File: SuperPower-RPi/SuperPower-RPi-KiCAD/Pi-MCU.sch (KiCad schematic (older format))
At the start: 25 parts, among them J5 Conn_01x06, J7 Conn_01x03, J8 Conn_01x10, J9 Conn_01x02, SW1 Tact, U3 STM32F412RETx, U4 ATtiny85-20SU, U5 ME6210A33M3G

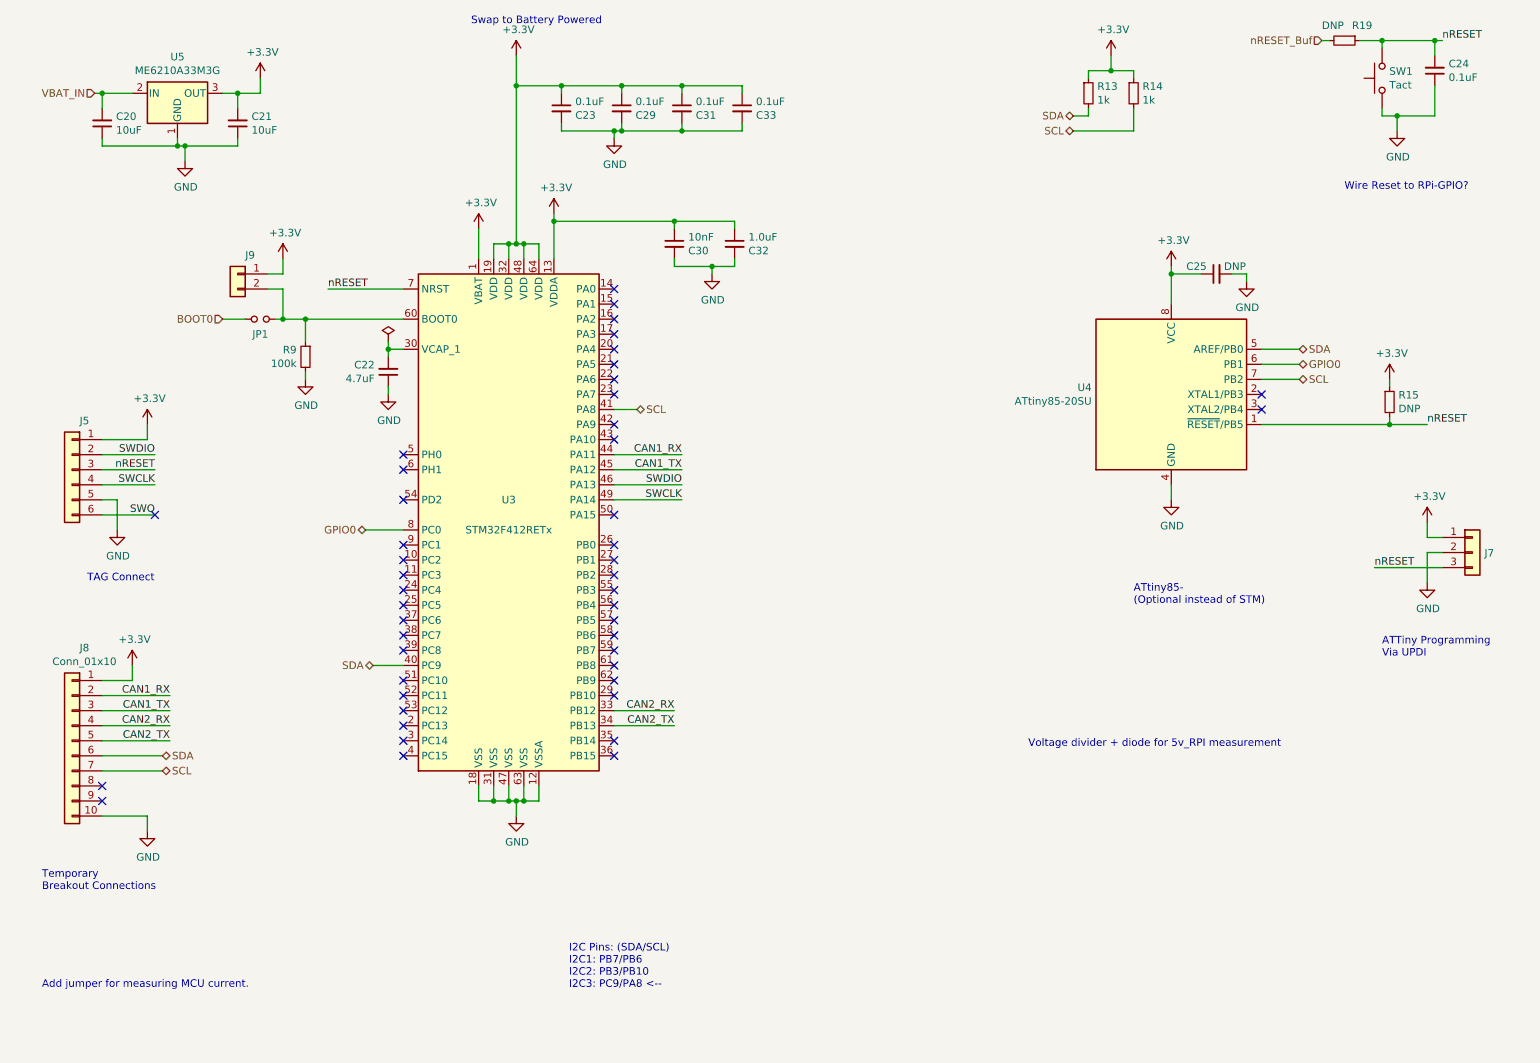
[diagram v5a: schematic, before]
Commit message: Added voltage divider to measure 5V rail.
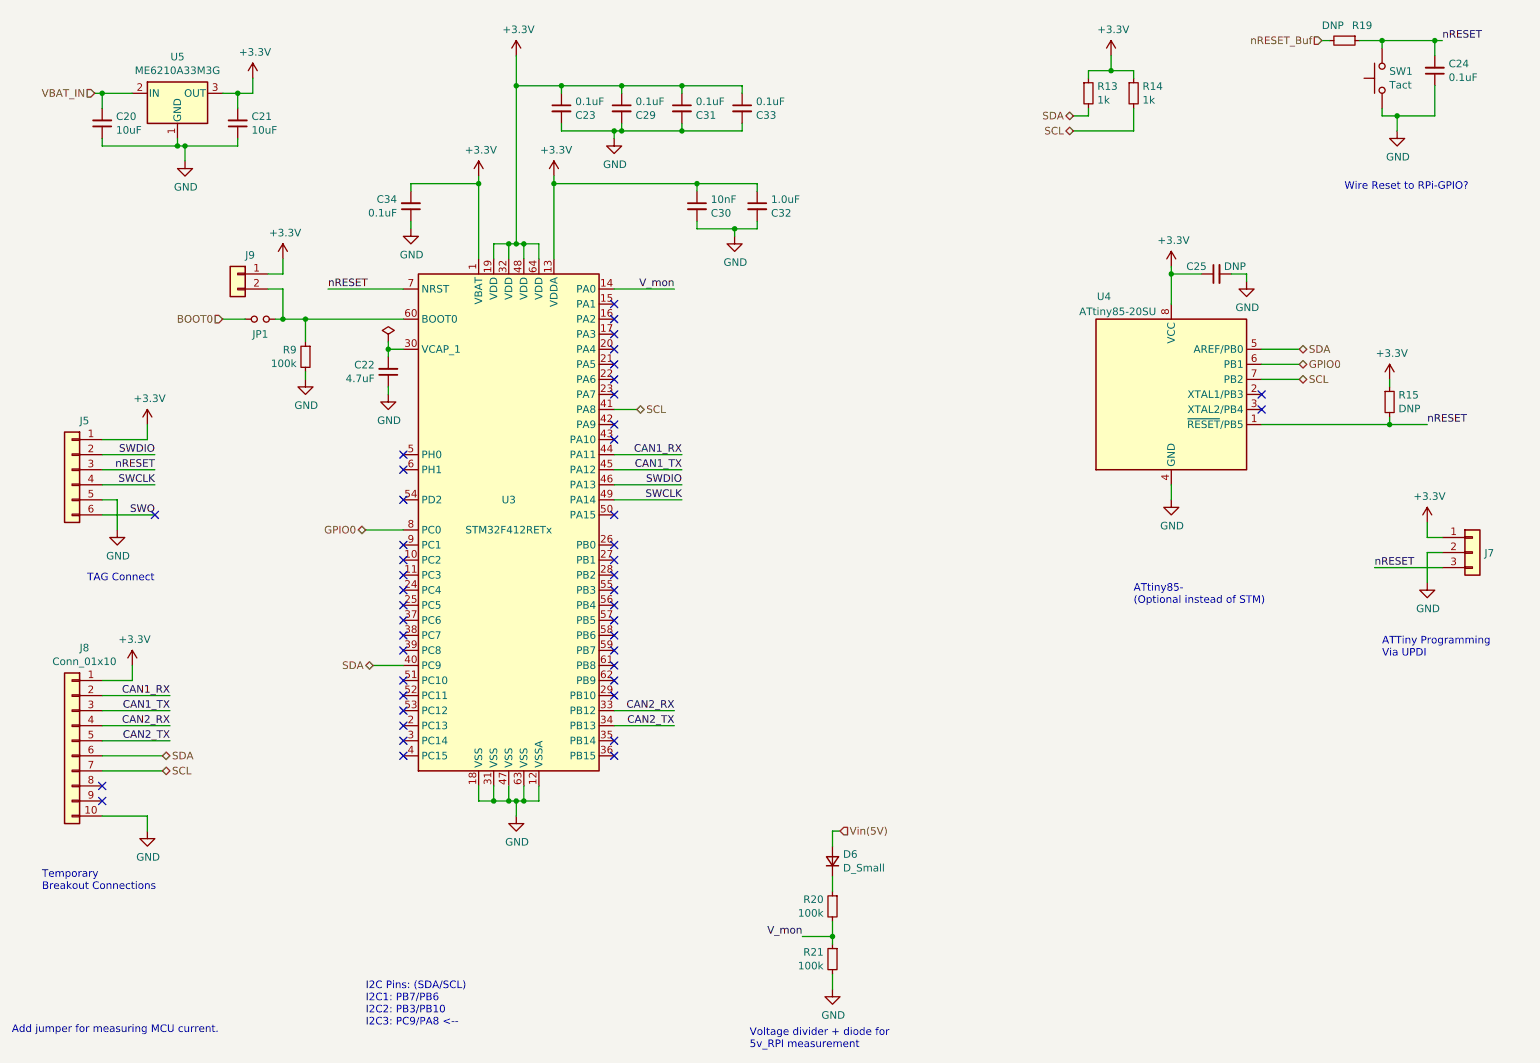
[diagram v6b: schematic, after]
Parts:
- added C34: 0.1uF, Capacitor_SMD:C_0603_1608Metric, symbol Device:C_Small
- added D6: D_Small, Diode_SMD:D_SOD-523, symbol Device:D_Small
- added R20, R21: 100k, Resistor_SMD:R_0603_1608Metric, symbol Device:R_Small
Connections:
- net +3V3: now also C34.2
- net GND: now also C34.1, R21.2
- net V_mon: now reaches U3.14 (PA0)
- net V_mon: now also R20.2, R21.1
- new net: D6.1 (K), R20.1
- new net Vin(5V): D6.2 (A)
- no-connect marks 46 -> 45
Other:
- note added: "Voltage divider + diode for\n5v_RPI measurement"
- note removed: "Swap to Battery Powered"
- note removed: "Voltage divider + diode for 5v_RPI measurement"
- moved on the sheet: C30, C32
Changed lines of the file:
@@
 $Descr A4 11693 8268
 encoding utf-8
-Sheet 6 8
+Sheet 8 8
 Title ""
 Date ""
@@
 Text HLabel 3150 4150 0    50   BiDi ~ 0
 GPIO0
-Text Notes 1000 7200 0    50   ~ 0
+Text Notes 800  7500 0    50   ~ 0
 Add jumper for measuring MCU current.
 Text HLabel 7850 1400 0    50   BiDi ~ 0
@@
 	-1   0    0    -1
 $EndComp
-Text Notes 4500 7200 0    50   ~ 0
+Text Notes 3150 7450 0    50   ~ 0
 I2C Pins: (SDA/SCL)\nI2C1: PB7/PB6\nI2C2: PB3/PB10\nI2C3: PC9/PA8 <--
 Wire Wire Line
@@
 NoConn ~ 4800 2750
 NoConn ~ 4800 2650
-NoConn ~ 4800 2550
 $Comp
 L power:GND #PWR021
@@
 L power:GND #PWR035
 U 1 1 5FAC45E3
-P 5450 2450
-F 0 "#PWR035" H 5450 2200 50  0001 C CNN
-F 1 "GND" H 5455 2277 50  0000 C CNN
-F 2 "" H 5450 2450 50  0001 C CNN
-F 3 "" H 5450 2450 50  0001 C CNN
-	1    5450 2450
+P 5600 2200
+F 0 "#PWR035" H 5600 1950 50  0001 C CNN
+F 1 "GND" H 5605 2027 50  0000 C CNN
+F 2 "" H 5600 2200 50  0001 C CNN
+F 3 "" H 5600 2200 50  0001 C CNN
+	1    5600 2200
 	1    0    0    -1
 $EndComp
@@
 L Device:C_Small C30
 U 1 1 5FADB8CB
-P 5200 2250
-F 0 "C30" H 5108 2204 50  0000 R CNN
-F 1 "10nF" H 5108 2295 50  0000 R CNN
-F 2 "Capacitor_SMD:C_0603_1608Metric" H 5200 2250 50  0001 C CNN
-F 3 "~" H 5200 2250 50  0001 C CNN
-	1    5200 2250
+P 5350 2000
+F 0 "C30" H 5258 1954 50  0000 R CNN
+F 1 "10nF" H 5258 2045 50  0000 R CNN
+F 2 "Capacitor_SMD:C_0603_1608Metric" H 5350 2000 50  0001 C CNN
+F 3 "~" H 5350 2000 50  0001 C CNN
+	1    5350 2000
 	-1   0    0    -1
 $EndComp
@@
 L Device:C_Small C32
 U 1 1 5FADBBC4
-P 5600 2250
-F 0 "C32" H 5508 2204 50  0000 R CNN
-F 1 "1.0uF" H 5508 2295 50  0000 R CNN
-F 2 "Capacitor_SMD:C_0603_1608Metric" H 5600 2250 50  0001 C CNN
-F 3 "~" H 5600 2250 50  0001 C CNN
-	1    5600 2250
+P 5750 2000
+F 0 "C32" H 5658 1954 50  0000 R CNN
+F 1 "1.0uF" H 5658 2045 50  0000 R CNN
+F 2 "Capacitor_SMD:C_0603_1608Metric" H 5750 2000 50  0001 C CNN
+F 3 "~" H 5750 2000 50  0001 C CNN
+	1    5750 2000
 	-1   0    0    -1
 $EndComp
@@
 $EndComp
 Wire Wire Line
-	4400 2050 4400 2100
-Wire Wire Line
-	4400 2100 5200 2100
-Wire Wire Line
-	5600 2100 5600 2150
-Connection ~ 4400 2100
-Wire Wire Line
-	4400 2100 4400 2350
-Wire Wire Line
-	5200 2150 5200 2100
-Connection ~ 5200 2100
-Wire Wire Line
-	5200 2100 5600 2100
-Wire Wire Line
-	5200 2350 5200 2400
-Wire Wire Line
-	5200 2400 5450 2400
-Wire Wire Line
-	5600 2400 5600 2350
-Wire Wire Line
-	5450 2450 5450 2400
-Connection ~ 5450 2400
-Wire Wire Line
-	5450 2400 5600 2400
+	5750 1850 5750 1900
+Wire Wire Line
+	5350 1900 5350 1850
+Connection ~ 5350 1850
+Wire Wire Line
+	5350 1850 5750 1850
+Wire Wire Line
+	5350 2100 5350 2150
+Wire Wire Line
+	5350 2150 5600 2150
+Wire Wire Line
+	5750 2150 5750 2100
+Wire Wire Line
+	5600 2200 5600 2150
+Connection ~ 5600 2150
+Wire Wire Line
+	5600 2150 5750 2150
 Wire Wire Line
 	4150 1200 4450 1200
@@
 Wire Wire Line
 	9350 2950 9100 2950
-$Comp
-L MCU_Microchip_ATtiny:ATtiny85-20SU U4
-U 1 1 5FAE2AC9
-P 8500 3250
-F 0 "U4" H 7971 3296 50  0000 R CNN
-F 1 "ATtiny85-20SU" H 7971 3205 50  0000 R CNN
-F 2 "Package_SO:SOIJ-8_5.3x5.3mm_P1.27mm" H 8500 3250 50  0001 C CIN
-F 3 "http://ww1.microchip.com/downloads/en/DeviceDoc/atmel-2586-avr-8-bit-microcontroller-attiny25-attiny45-attiny85_datasheet.pdf" H 8500 3250 50  0001 C CNN
-	1    8500 3250
-	1    0    0    -1
-$EndComp
 Wire Wire Line
 	9100 3450 9950 3450
 NoConn ~ 9100 3350
 NoConn ~ 9100 3250
-Text Notes 7550 5600 0    50   ~ 0
-Voltage divider + diode for 5v_RPI measurement
-Text Notes 3850 800  0    50   ~ 0
-Swap to Battery Powered
+Text Notes 5700 7600 0    50   ~ 0
+Voltage divider + diode for\n5v_RPI measurement
 Text HLabel 2200 2750 0    50   Input ~ 0
 BOOT0
@@
 L power:+3.3V #PWR033
 U 1 1 5FB28CED
-P 4400 2050
-F 0 "#PWR033" H 4400 1900 50  0001 C CNN
-F 1 "+3.3V" H 4415 2223 50  0000 C CNN
-F 2 "" H 4400 2050 50  0001 C CNN
-F 3 "" H 4400 2050 50  0001 C CNN
-	1    4400 2050
+P 4400 1800
+F 0 "#PWR033" H 4400 1650 50  0001 C CNN
+F 1 "+3.3V" H 4415 1973 50  0000 C CNN
+F 2 "" H 4400 1800 50  0001 C CNN
+F 3 "" H 4400 1800 50  0001 C CNN
+	1    4400 1800
 	1    0    0    -1
 $EndComp
@@
 $EndComp
 $Comp
-L power:+3.3V #PWR?
+L power:+3.3V #PWR016
 U 1 1 5FB90BA7
-P 2450 1150
-F 0 "#PWR?" H 2450 1000 50  0001 C CNN
-F 1 "+3.3V" H 2465 1323 50  0000 C CNN
-F 2 "" H 2450 1150 50  0001 C CNN
-F 3 "" H 2450 1150 50  0001 C CNN
-	1    2450 1150
-	1    0    0    -1
-$EndComp
-Wire Wire Line
-	2450 1250 2450 1150
-$Comp
-L power:+3.3V #PWR?
+P 2400 1150
+F 0 "#PWR016" H 2400 1000 50  0001 C CNN
+F 1 "+3.3V" H 2415 1323 50  0000 C CNN
+F 2 "" H 2400 1150 50  0001 C CNN
+F 3 "" H 2400 1150 50  0001 C CNN
+	1    2400 1150
+	1    0    0    -1
+$EndComp
+$Comp
+L power:+3.3V #PWR037
 U 1 1 5FB98D8D
-P 3900 2150
-F 0 "#PWR?" H 3900 2000 50  0001 C CNN
-F 1 "+3.3V" H 3915 2323 50  0000 C CNN
-F 2 "" H 3900 2150 50  0001 C CNN
-F 3 "" H 3900 2150 50  0001 C CNN
-	1    3900 2150
-	1    0    0    -1
-$EndComp
-Wire Wire Line
-	3900 2150 3900 2350
+P 3900 1800
+F 0 "#PWR037" H 3900 1650 50  0001 C CNN
+F 1 "+3.3V" H 3915 1973 50  0000 C CNN
+F 2 "" H 3900 1800 50  0001 C CNN
+F 3 "" H 3900 1800 50  0001 C CNN
+	1    3900 1800
+	1    0    0    -1
+$EndComp
+Wire Wire Line
+	3900 1800 3900 1850
 Connection ~ 2300 1250
-Wire Wire Line
-	2300 1250 2450 1250
+$Comp
+L Device:R_Small R21
+U 1 1 5FAAB54D
+P 6250 7000
+F 0 "R21" H 6309 7046 50  0000 L CNN
+F 1 "100k" H 6309 6955 50  0000 L CNN
+F 2 "Resistor_SMD:R_0603_1608Metric" H 6250 7000 50  0001 C CNN
+F 3 "~" H 6250 7000 50  0001 C CNN
+	1    6250 7000
+	-1   0    0    -1
+$EndComp
+$Comp
+L Device:R_Small R20
+U 1 1 5FAAC000
+P 6250 6650
+F 0 "R20" H 6309 6696 50  0000 L CNN
+F 1 "100k" H 6309 6605 50  0000 L CNN
+F 2 "Resistor_SMD:R_0603_1608Metric" H 6250 6650 50  0001 C CNN
+F 3 "~" H 6250 6650 50  0001 C CNN
+	1    6250 6650
+	-1   0    0    -1
+$EndComp
+$Comp
+L power:GND #PWR038
+U 1 1 5FAAC254
+P 6250 7200
+F 0 "#PWR038" H 6250 6950 50  0001 C CNN
+F 1 "GND" H 6255 7027 50  0000 C CNN
+F 2 "" H 6250 7200 50  0001 C CNN
+F 3 "" H 6250 7200 50  0001 C CNN
+	1    6250 7200
+	1    0    0    -1
+$EndComp
+Wire Wire Line
+	6250 7200 6250 7100
+Wire Wire Line
+	6250 6900 6250 6850
+$Comp
+L Device:D_Small D6
+U 1 1 5FAB9400
+P 6250 6350
+F 0 "D6" V 6296 6280 50  0000 R CNN
+F 1 "D_Small" V 6205 6280 50  0000 R CNN
+F 2 "Diode_SMD:D_SOD-523" V 6250 6350 50  0001 C CNN
+F 3 "~" V 6250 6350 50  0001 C CNN
+F 4 "FIX FOOTPRINT" H 6250 6350 50  0001 C CNN "Mfg"
+	1    6250 6350
+	0    -1   -1   0
+$EndComp
+Wire Wire Line
+	6250 6550 6250 6450
+Text HLabel 6300 6150 2    50   Input ~ 0
+Vin(5V)
+Wire Wire Line
+	6250 6250 6250 6150
+Wire Wire Line
+	6250 6150 6300 6150
+Text Label 6050 6850 2    50   ~ 0
+V_mon
+Wire Wire Line
+	6050 6850 6250 6850
+Connection ~ 6250 6850
+Wire Wire Line
+	6250 6850 6250 6750
+Text Label 5200 2550 2    50   ~ 0
+V_mon
+Wire Wire Line
+	4400 1800 4400 1850
+Wire Wire Line
+	4400 1850 5350 1850
+Wire Wire Line
+	4800 2550 5200 2550
+$Comp
+L MCU_Microchip_ATtiny:ATtiny85-20SU U4
+U 1 1 5FAE2AC9
+P 8500 3250
+F 0 "U4" H 8100 3900 50  0000 R CNN
+F 1 "ATtiny85-20SU" H 8400 3800 50  0000 R CNN
+F 2 "Package_SO:SOIJ-8_5.3x5.3mm_P1.27mm" H 8500 3250 50  0001 C CIN
+F 3 "http://ww1.microchip.com/downloads/en/DeviceDoc/atmel-2586-avr-8-bit-microcontroller-attiny25-attiny45-attiny85_datasheet.pdf" H 8500 3250 50  0001 C CNN
+	1    8500 3250
+	1    0    0    -1
+$EndComp
+$Comp
+L Device:C_Small C34
+U 1 1 5FAFC531
+P 3450 2000
+F 0 "C34" H 3358 1954 50  0000 R CNN
+F 1 "0.1uF" H 3358 2045 50  0000 R CNN
+F 2 "Capacitor_SMD:C_0603_1608Metric" H 3450 2000 50  0001 C CNN
+F 3 "~" H 3450 2000 50  0001 C CNN
+	1    3450 2000
+	1    0    0    1
+$EndComp
+Wire Wire Line
+	2400 1250 2400 1150
+Wire Wire Line
+	2300 1250 2400 1250
+Wire Wire Line
+	3900 1850 3450 1850
+Wire Wire Line
+	3450 1850 3450 1900
+Connection ~ 3900 1850
+Wire Wire Line
+	3900 1850 3900 2350
+$Comp
+L power:GND #PWR0113
+U 1 1 5FB5DC98
+P 3450 2150
+F 0 "#PWR0113" H 3450 1900 50  0001 C CNN
+F 1 "GND" H 3455 1977 50  0000 C CNN
+F 2 "" H 3450 2150 50  0001 C CNN
+F 3 "" H 3450 2150 50  0001 C CNN
+	1    3450 2150
+	1    0    0    -1
+$EndComp
+Wire Wire Line
+	3450 2150 3450 2100
+Connection ~ 4400 1850
+Wire Wire Line
+	4400 1850 4400 2350
 $EndSCHEMATC

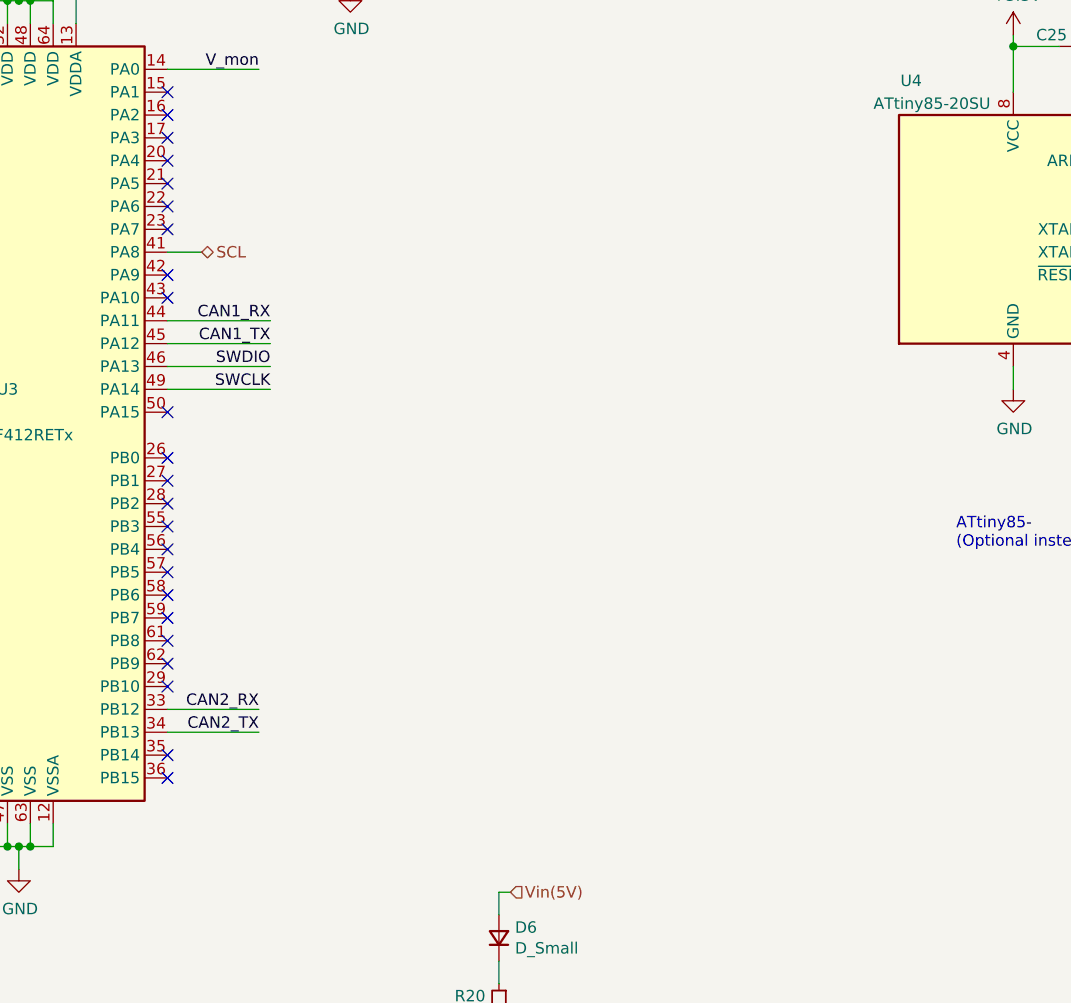
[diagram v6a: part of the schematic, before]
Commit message: Added DotStar to MCU page, and a jumper to Boost converter Enable pin.
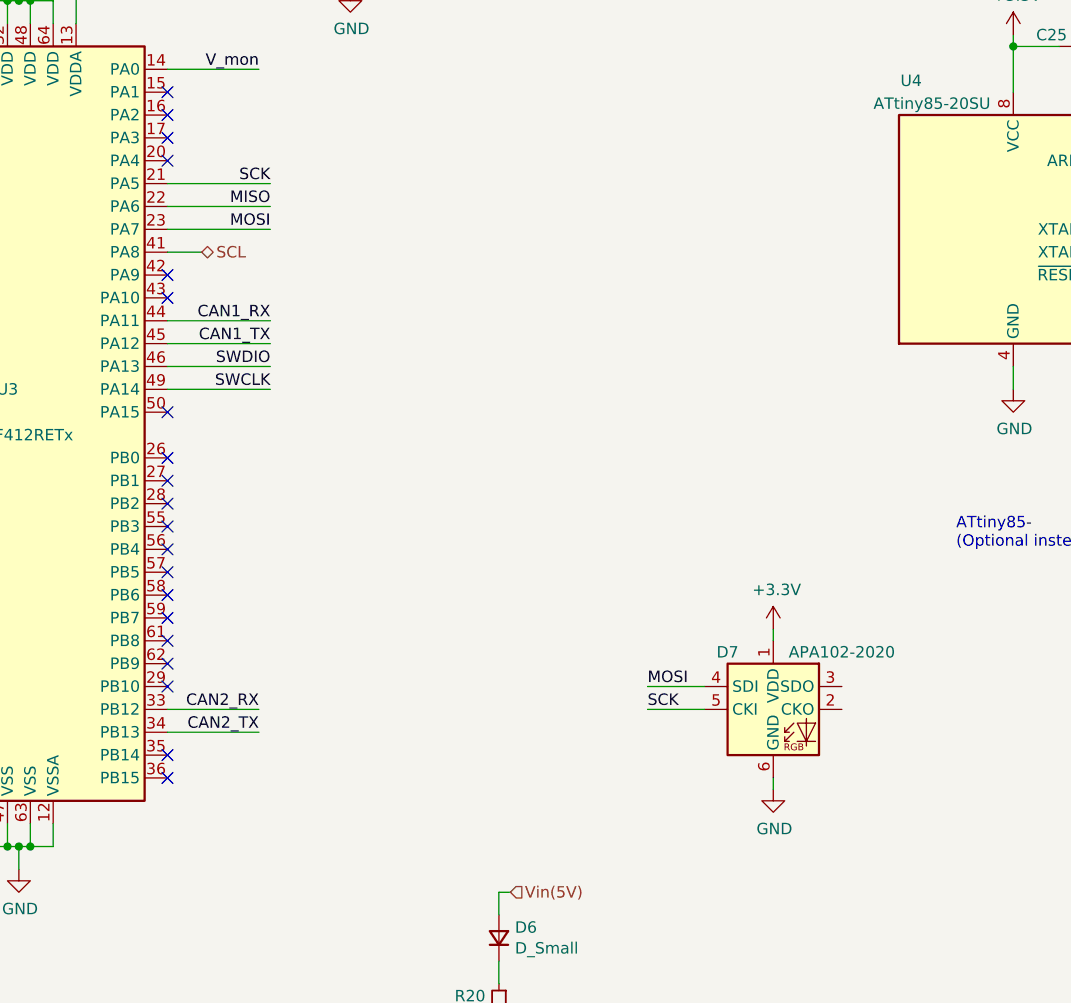
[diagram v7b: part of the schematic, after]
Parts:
- added D7: APA102-2020, LED_SMD:LED-APA102-2020, symbol LED:APA102-2020
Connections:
- net +3V3: now also D7.1 (VDD)
- net GND: now also D7.6 (GND)
- net SCK: now reaches U3.21 (PA5)
- net SCK: now also D7.5 (CKI)
- net MISO: now reaches U3.22 (PA6)
- net MOSI: now reaches U3.23 (PA7)
- net MOSI: now also D7.4 (SDI)
- no-connect marks 45 -> 42
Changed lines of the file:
@@
 NoConn ~ 4800 3550
 NoConn ~ 4800 3450
-NoConn ~ 4800 3250
-NoConn ~ 4800 3150
-NoConn ~ 4800 3050
 NoConn ~ 4800 2950
 NoConn ~ 4800 2850
@@
 Wire Wire Line
 	4400 1850 4400 2350
+$Comp
+L LED:APA102-2020 D7
+U 1 1 5FBB8F09
+P 7450 5350
+F 0 "D7" H 7250 5600 50  0000 C CNN
+F 1 "APA102-2020" H 7750 5600 50  0000 C CNN
+F 2 "LED_SMD:LED-APA102-2020" H 7500 5050 50  0001 L TNN
+F 3 "http://www.led-color.com/upload/201604/APA102-2020%20SMD%20LED.pdf" H 7550 4975 50  0001 L TNN
+	1    7450 5350
+	1    0    0    -1
+$EndComp
+Wire Wire Line
+	4800 3050 5250 3050
+Wire Wire Line
+	4800 3250 5250 3250
+Wire Wire Line
+	5250 3150 4800 3150
+Text Label 5250 3050 2    50   ~ 0
+SCK
+Text Label 5250 3150 2    50   ~ 0
+MISO
+Text Label 5250 3250 2    50   ~ 0
+MOSI
+Text Label 6900 5350 0    50   ~ 0
+SCK
+Wire Wire Line
+	6900 5350 7150 5350
+$Comp
+L power:GND #PWR041
+U 1 1 5FBD9F61
+P 7450 5700
+F 0 "#PWR041" H 7450 5450 50  0001 C CNN
+F 1 "GND" H 7455 5527 50  0000 C CNN
+F 2 "" H 7450 5700 50  0001 C CNN
+F 3 "" H 7450 5700 50  0001 C CNN
+	1    7450 5700
+	1    0    0    -1
+$EndComp
+Wire Wire Line
+	7450 5700 7450 5650
+Text Label 6900 5250 0    50   ~ 0
+MOSI
+Wire Wire Line
+	6900 5250 7150 5250
+$Comp
+L power:+3.3V #PWR040
+U 1 1 5FBF1DAE
+P 7450 5000
+F 0 "#PWR040" H 7450 4850 50  0001 C CNN
+F 1 "+3.3V" H 7465 5173 50  0000 C CNN
+F 2 "" H 7450 5000 50  0001 C CNN
+F 3 "" H 7450 5000 50  0001 C CNN
+	1    7450 5000
+	1    0    0    -1
+$EndComp
+Wire Wire Line
+	7450 5000 7450 5050
 $EndSCHEMATC
